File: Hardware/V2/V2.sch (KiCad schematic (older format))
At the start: 66 parts, among them J1 USB_B_Mini, J2 I2C_OLED, J3 ICSP, Q1 MMBT2222, SW1 SW_Push_Dual, SW2 B2, SW3 B1, U1 ATmega32U4-AU, U2 LIS3DH, U3 DHT11, U4 AP2112K-3.3, Y1 16Mhz

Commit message: Huellas asignadas
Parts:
- removed SW1: SW_Push_Dual, symbol Switch:SW_Push_Dual
- removed SW2: B2, symbol Switch:SW_Push_Dual
- removed SW3: B1, symbol Switch:SW_Push_Dual
- removed Y1: 16Mhz, symbol device:Resonator_Small
- added C18, C19: 22pF, Capacitor_SMD:C_0805_2012Metric, symbol device:C_Small
- added SW1: SW_Push, Button_Switch_THT:SW_PUSH_6mm, symbol Switch:SW_Push
- added SW2, SW3: SW_Push, Button_Switch_THT:SW_PUSH-12mm, symbol Switch:SW_Push
- added Y1: 16MHz, Crystal:Crystal_HC49-4H_Vertical, symbol device:Crystal_Small
- BZ1: footprint (none) -> eduardu:BUZZER-PB1240
- C1, C10, C11, C12, C13, C14, C15, C16, C17, C3, C4, C5, C6, C7, C8, C9: footprint (none) -> Capacitor_SMD:C_0805_2012Metric
- C2: footprint (none) -> Capacitor_SMD:C_1206_3216Metric
- D10, D11, D8, D9: footprint (none) -> LED_THT:LED_D5.0mm
- D13, D14: footprint (none) -> LED_SMD:LED_0805_2012Metric
- D3: footprint (none) -> Diode_SMD:D_SOD-123
- J1: footprint (none) -> Connector_USB:USB_Mini-B_Lumberg_2486_01_Horizontal
- J2, U3: footprint (none) -> Connector_PinHeader_2.54mm:PinHeader_1x04_P2.54mm_Vertical
- J3: footprint (none) -> Connector_PinHeader_2.54mm:PinHeader_2x03_P2.54mm_Vertical
- Q1: footprint (none) -> Package_TO_SOT_SMD:SOT-23
- R1, R11, R12, R13, R14, R15, R16, R17, R18, R19, R2, R20, R3, R4, R5, R6, R7, R8, R9: footprint (none) -> Resistor_SMD:R_0805_2012Metric
- R10: footprint (none) -> OptoDevice:R_LDR_4.9x4.2mm_P2.54mm_Vertical
- RV1: footprint (none) -> Potentiometer_THT:Potentiometer_Techtalents
- S1: footprint JOYSTICK -> eduardu:JOYSTICK
- U2: footprint LGA-16-3X3 -> Package_LGA:LGA-16_3x3mm_P0.5mm_LayoutBorder3x5y
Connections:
- wire segments 265 -> 255

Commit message: Comenzando la placa
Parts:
- added D15: 1N4148, Diode_SMD:D_SOD-123, symbol device:D_Small
- added J4: BT_CONN, Connector_PinHeader_2.54mm:PinHeader_1x06_P2.54mm_Vertical, symbol Connector:Conn_01x06_Female
- added J5: BAT, Connector_JST:JST_PH_S2B-PH-SM4-TB_1x02-1MP_P2.00mm_Horizontal, symbol Connector_Generic:Conn_01x02
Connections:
- net GND: now also J4.4 (Pin_4), J5.2 (Pin_2)
- net SCL: no longer J2.4 (Pin_4), R4.1, U1.19 (PD1), U2.6 (SDA/SDI)
- net VUSB: now also D15.1 (K)
- new net: D15.2 (A), J5.1 (Pin_1)
- new net +5V: J4.5 (Pin_5)
- new net BT_RX: J4.2 (Pin_2)
- new net BT_TX: J4.3 (Pin_3)
- new net KEY: J4.6 (Pin_6)
- new net SDA: J2.4 (Pin_4), R4.1, U1.19 (PD1), U2.6 (SDA/SDI)
- new net STATE: J4.1 (Pin_1)
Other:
- note added: "BLUETOOTH"
- moved on the sheet: C14, C15, C16, C17, U4

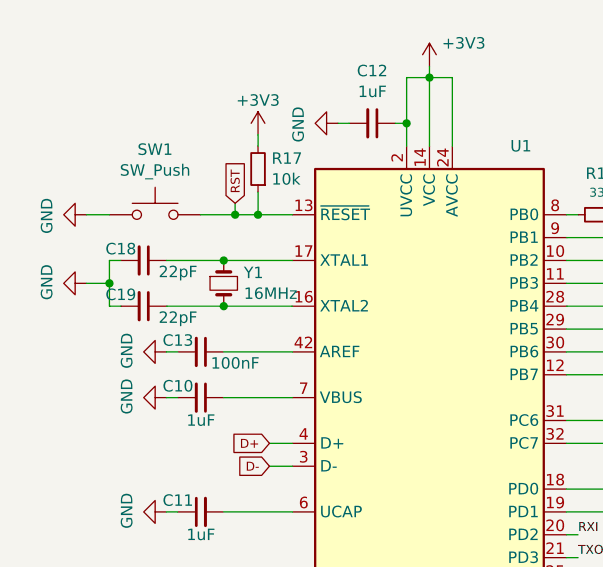
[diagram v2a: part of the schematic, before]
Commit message: Componentes colocados
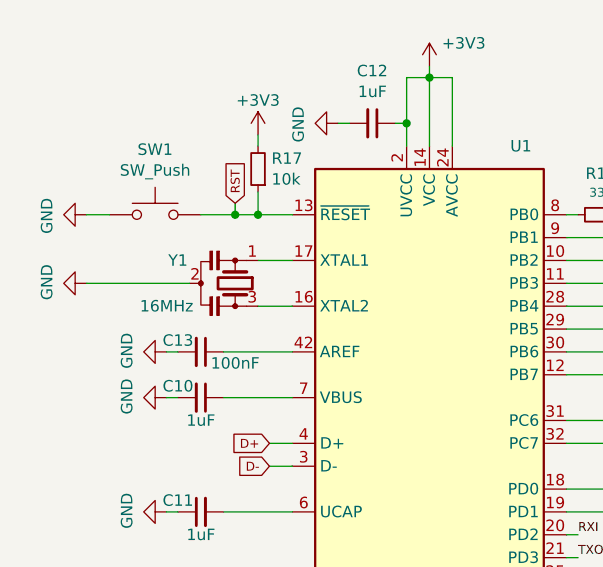
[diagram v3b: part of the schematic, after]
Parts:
- removed C18, C19: 22pF, Capacitor_SMD:C_0805_2012Metric, symbol device:C_Small
- removed Y1: 16MHz, Crystal:Crystal_HC49-4H_Vertical, symbol device:Crystal_Small
- added Y1: 16MHz, lib_fp:RESONATOR-SMD-3.2X1.3, symbol device:Resonator_Small
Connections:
- net GND: now also Y1.2
- net at U1.16 (XTAL2): now also Y1.3
- net at U1.17 (XTAL1): now also Y1.1
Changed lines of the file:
@@
 Wire Wire Line
 	1300 1850 1450 1850
-$Comp
-L device:C_Small C18
-U 1 1 5C96B953
-P 1050 2050
-F 0 "C18" V 1000 1950 50  0000 C CNN
-F 1 "22pF" V 1100 2200 50  0000 C CNN
-F 2 "Capacitor_SMD:C_0805_2012Metric" H 1050 2050 50  0001 C CNN
-F 3 "~" H 1050 2050 50  0001 C CNN
-	1    1050 2050
-	0    1    1    0
-$EndComp
-$Comp
-L device:Crystal_Small Y1
-U 1 1 5C96D7B0
-P 1400 2150
-F 0 "Y1" V 1354 2238 50  0000 L CNN
-F 1 "16MHz" V 1445 2238 50  0000 L CNN
-F 2 "Crystal:Crystal_HC49-4H_Vertical" H 1400 2150 50  0001 C CNN
-F 3 "~" H 1400 2150 50  0001 C CNN
-	1    1400 2150
-	0    1    1    0
-$EndComp
-$Comp
-L device:C_Small C19
-U 1 1 5C96ED3B
-P 1050 2250
-F 0 "C19" V 1000 2150 50  0000 C CNN
-F 1 "22pF" V 1100 2400 50  0000 C CNN
-F 2 "Capacitor_SMD:C_0805_2012Metric" H 1050 2250 50  0001 C CNN
-F 3 "~" H 1050 2250 50  0001 C CNN
-	1    1050 2250
-	0    1    1    0
-$EndComp
-Wire Wire Line
-	800  2150 900  2150
-Wire Wire Line
-	900  2150 900  2050
-Wire Wire Line
-	900  2050 950  2050
-Wire Wire Line
-	900  2150 900  2250
-Wire Wire Line
-	900  2250 950  2250
-Connection ~ 900  2150
-Wire Wire Line
-	1150 2250 1400 2250
-Wire Wire Line
-	1400 2250 1700 2250
-Connection ~ 1400 2250
-Wire Wire Line
-	1400 2050 1700 2050
-Wire Wire Line
-	1400 2050 1150 2050
-Connection ~ 1400 2050
 Text Notes 650  4900 0    79   ~ 0
 BLUETOOTH
@@
 Wire Wire Line
 	6200 1300 6200 1700
+$Comp
+L device:Resonator_Small Y1
+U 1 1 5C93DA74
+P 1450 2150
+F 0 "Y1" V 1350 1900 50  0000 C CNN
+F 1 "16MHz" V 1550 1850 50  0000 C CNN
+F 2 "lib_fp:RESONATOR-SMD-3.2X1.3" H 1425 2150 50  0001 C CNN
+F 3 "~" H 1425 2150 50  0001 C CNN
+	1    1450 2150
+	0    1    1    0
+$EndComp
+Wire Wire Line
+	1550 2050 1700 2050
+Wire Wire Line
+	1550 2250 1700 2250
+Wire Wire Line
+	800  2150 1250 2150
 $EndSCHEMATC

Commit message: Cambio de forma
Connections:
- net +5V is gone; now on net +3V3: J4.5 (Pin_5)
- net BT_RX: now also U1.21 (PD3)
- net BT_TX: now also U1.20 (PD2)
- net RXI: no longer U1.20 (PD2)
- net TXO: no longer U1.21 (PD3)
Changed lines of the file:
@@
 Wire Wire Line
 	2900 3250 2950 3250
-Text Label 2950 3250 0    39   ~ 0
+Text Label 3250 3300 0    39   ~ 0
 RXI
-Text Label 2950 3350 0    39   ~ 0
+Text Label 3250 3400 0    39   ~ 0
 TXO
 Text Notes 3450 3200 2    39   ~ 0
@@
 Wire Wire Line
 	650  5350 1150 5350
-$Comp
-L power:+5V #PWR028
-U 1 1 5CA48945
-P 600 5150
-F 0 "#PWR028" H 600 5000 50  0001 C CNN
-F 1 "+5V" H 615 5323 50  0000 C CNN
-F 2 "" H 600 5150 50  0001 C CNN
-F 3 "" H 600 5150 50  0001 C CNN
-	1    600  5150
-	1    0    0    -1
-$EndComp
 Wire Wire Line
 	600  5150 600  5450
@@
 Wire Wire Line
 	800  2150 1250 2150
+Text GLabel 2950 3350 2    39   Input ~ 0
+BT_RX
+Text GLabel 2950 3250 2    39   Input ~ 0
+BT_TX
+$Comp
+L power:+3V3 #PWR?
+U 1 1 5C9786A5
+P 600 5150
+F 0 "#PWR?" H 600 5000 50  0001 C CNN
+F 1 "+3V3" H 600 5300 50  0000 C CNN
+F 2 "" H 600 5150 50  0001 C CNN
+F 3 "" H 600 5150 50  0001 C CNN
+	1    600  5150
+	1    0    0    -1
+$EndComp
 $EndSCHEMATC

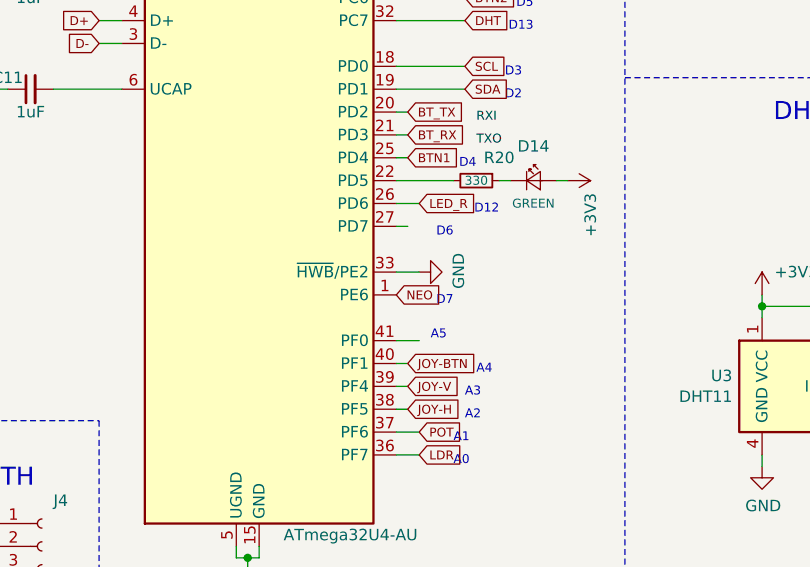
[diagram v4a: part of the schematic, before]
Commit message: Taladros del Slider ensanchados
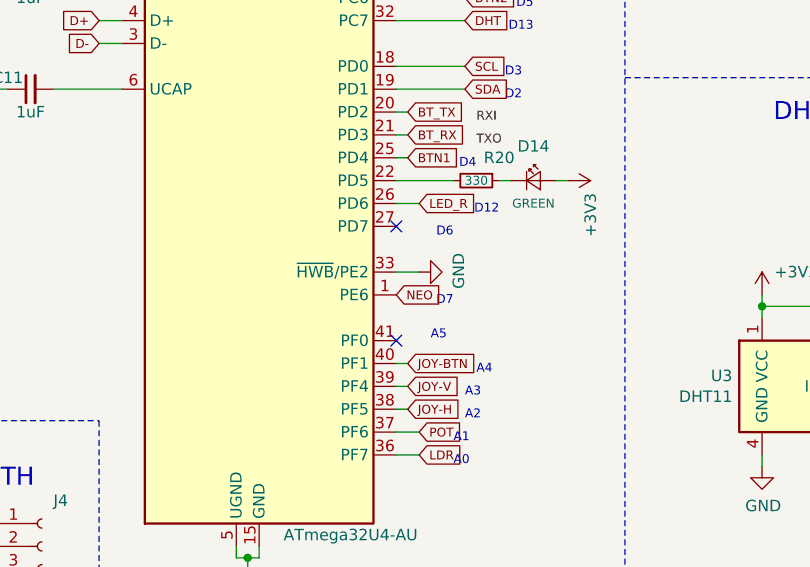
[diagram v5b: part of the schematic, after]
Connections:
- no-connect marks 6 -> 8
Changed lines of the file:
@@
 A5
-Wire Wire Line
-	2900 4250 3000 4250
 Wire Wire Line
 	2900 4650 3000 4650
@@
 Text Notes 3150 3800 2    39   ~ 0
 D6
-Wire Wire Line
-	2900 3750 2950 3750
 Text Notes 3350 3700 2    39   ~ 0
 D12
@@
 BT_TX
 $Comp
-L power:+3V3 #PWR?
+L power:+3V3 #PWR0125
 U 1 1 5C9786A5
 P 600 5150
-F 0 "#PWR?" H 600 5000 50  0001 C CNN
+F 0 "#PWR0125" H 600 5000 50  0001 C CNN
 F 1 "+3V3" H 600 5300 50  0000 C CNN
 F 2 "" H 600 5150 50  0001 C CNN
@@
 	1    0    0    -1
 $EndComp
+NoConn ~ 2900 3750
+NoConn ~ 2900 4250
 $EndSCHEMATC
